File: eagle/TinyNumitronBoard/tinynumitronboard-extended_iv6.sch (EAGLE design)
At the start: 39 parts

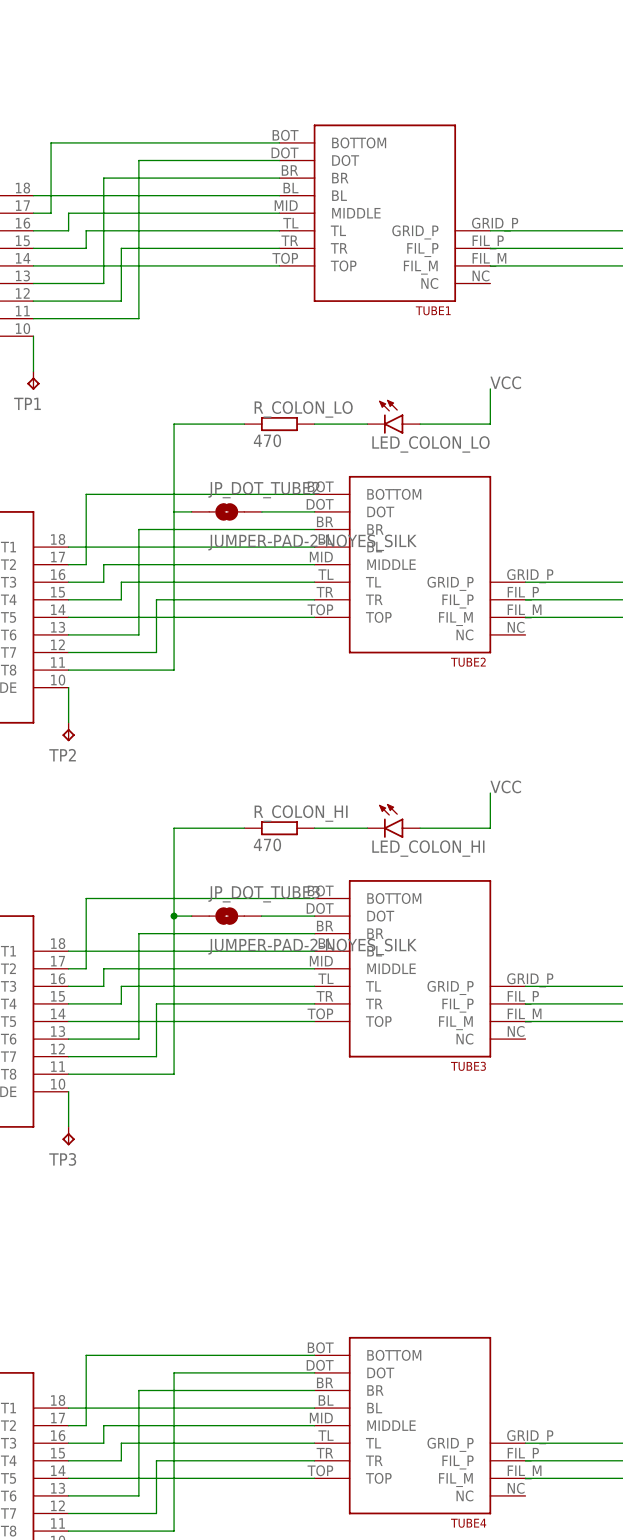
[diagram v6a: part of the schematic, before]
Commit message: added solder pad for dot for all tubes
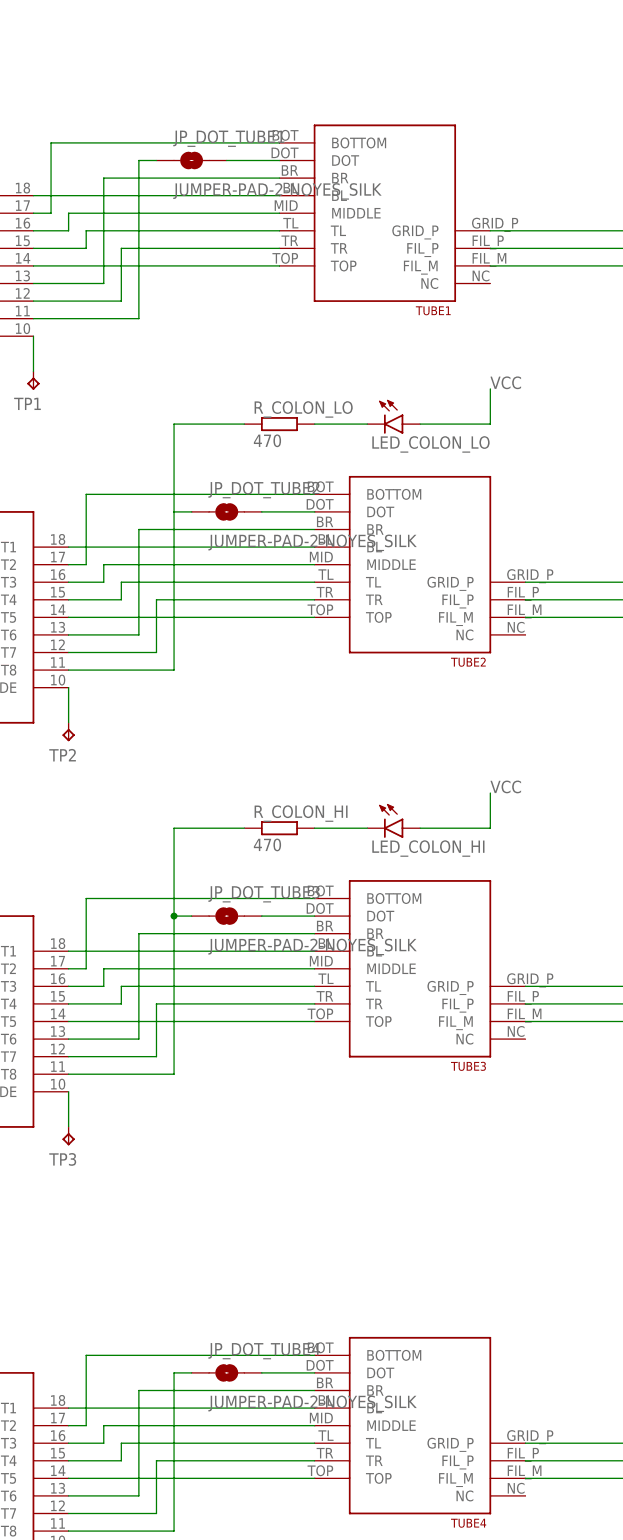
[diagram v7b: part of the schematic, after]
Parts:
- added JP_DOT_TUBE1, JP_DOT_TUBE4: JUMPER-PAD-2-NOYES_SILK, SparkFun-Passives:JUMPER-PAD-2-NOYES_SILK
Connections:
- new net N$79: JP_DOT_TUBE1.2, TUBE1.DOT
- new net N$80: JP_DOT_TUBE4.2, TUBE4.DOT
- net N$31: now also JP_DOT_TUBE4.1; no longer TUBE4.DOT
- net N$59: now also JP_DOT_TUBE1.1; no longer TUBE1.DOT
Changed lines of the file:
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@@
 <part name="TP3" library="testpad" deviceset="TP" device="B2,54" value="TPB2,54"/>
 <part name="TP4" library="testpad" deviceset="TP" device="B2,54" value="TPB2,54"/>
+<part name="JP_DOT_TUBE1" library="SparkFun-Passives" deviceset="JUMPER-PAD-2-NO" device="YES_SILK" value="JUMPER-PAD-2-NOYES_SILK"/>
+<part name="JP_DOT_TUBE4" library="SparkFun-Passives" deviceset="JUMPER-PAD-2-NO" device="YES_SILK" value="JUMPER-PAD-2-NOYES_SILK"/>
 </parts>
 <sheets>
@@
 <instance part="TP3" gate="G$1" x="20.32" y="-76.2" rot="R180"/>
 <instance part="TP4" gate="G$1" x="20.32" y="-139.7" rot="R180"/>
+<instance part="JP_DOT_TUBE1" gate="G$1" x="38.1" y="66.04"/>
+<instance part="JP_DOT_TUBE4" gate="G$1" x="43.18" y="-109.22"/>
 </instances>
 <busses>
@@
 <wire x1="15.24" y1="43.18" x2="30.48" y2="43.18" width="0.1524" layer="91"/>
 <wire x1="30.48" y1="43.18" x2="30.48" y2="66.04" width="0.1524" layer="91"/>
-<pinref part="TUBE1" gate="G$1" pin="DOT"/>
-<wire x1="30.48" y1="66.04" x2="50.8" y2="66.04" width="0.1524" layer="91"/>
+<pinref part="JP_DOT_TUBE1" gate="G$1" pin="1"/>
+<wire x1="30.48" y1="66.04" x2="33.02" y2="66.04" width="0.1524" layer="91"/>
 </segment>
 </net>
@@
 <wire x1="20.32" y1="-132.08" x2="35.56" y2="-132.08" width="0.1524" layer="91"/>
 <wire x1="35.56" y1="-132.08" x2="35.56" y2="-109.22" width="0.1524" layer="91"/>
-<pinref part="TUBE4" gate="G$1" pin="DOT"/>
-<wire x1="35.56" y1="-109.22" x2="55.88" y2="-109.22" width="0.1524" layer="91"/>
+<pinref part="JP_DOT_TUBE4" gate="G$1" pin="1"/>
+<wire x1="35.56" y1="-109.22" x2="38.1" y2="-109.22" width="0.1524" layer="91"/>
 </segment>
 </net>
@@
 </segment>
 </net>
+<net name="N$79" class="0">
+<segment>
+<pinref part="JP_DOT_TUBE1" gate="G$1" pin="2"/>
+<pinref part="TUBE1" gate="G$1" pin="DOT"/>
+<wire x1="43.18" y1="66.04" x2="50.8" y2="66.04" width="0.1524" layer="91"/>
+</segment>
+</net>
+<net name="N$80" class="0">
+<segment>
+<pinref part="JP_DOT_TUBE4" gate="G$1" pin="2"/>
+<pinref part="TUBE4" gate="G$1" pin="DOT"/>
+<wire x1="48.26" y1="-109.22" x2="55.88" y2="-109.22" width="0.1524" layer="91"/>
+</segment>
+</net>

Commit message: Crapped up, now fixing
Started version 2, ripped up everything
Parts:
- removed DRIVER2: ULN2803, uln2803:ULN2803
- removed TP1, TP2, TP3, TP4: TPB2,54, testpad:TPB2,54
- added IC1: IC_TD62783-SO-18W, dp_devices:IC_TD62783-SO-18W
- JP_INPUT, JP_OUTPUT: device SparkFun:M06SIP -> SparkFun-Connectors:CONN_05NO_SILK
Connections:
- removed net DIODE: DRIVER1.DIODE, DRIVER2.DIODE, DRIVER3.DIODE, DRIVER4.DIODE, TP1.TP, TP2.TP, TP3.TP, TP4.TP
- net GND: now also IC1.GND; no longer DRIVER2.GND
- net GRID_P: now also IC1.VS
- net N$14: now also IC1.OUT2; no longer DRIVER2.OUT1
- net N$16: now also IC1.OUT1; no longer DRIVER2.OUT2
- net N$17: now also IC1.OUT3; no longer DRIVER2.OUT3
- net N$21: no longer JP_OUTPUT.6
- net N$39: now also IC1.OUT4; no longer DRIVER2.OUT4
- net N$40: now also IC1.OUT5; no longer DRIVER2.OUT5
- net N$41: now also IC1.OUT6; no longer DRIVER2.OUT6
- net N$42: now also IC1.OUT7; no longer DRIVER2.OUT7
- net N$43: now also IC1.OUT8; no longer DRIVER2.OUT8
- net N$44: now also IC1.IN1; no longer DRIVER2.IN1
- net N$45: now also IC1.IN2; no longer DRIVER2.IN2
- net N$46: now also IC1.IN3; no longer DRIVER2.IN3
- net N$47: now also IC1.IN4; no longer DRIVER2.IN4
- net N$48: now also IC1.IN5; no longer DRIVER2.IN5
- net N$49: now also IC1.IN6; no longer DRIVER2.IN6
- net N$50: now also IC1.IN7; no longer DRIVER2.IN7
- net N$51: now also IC1.IN8; no longer DRIVER2.IN8
- net SER: no longer JP_INPUT.6
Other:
- note removed: "CARRY"
